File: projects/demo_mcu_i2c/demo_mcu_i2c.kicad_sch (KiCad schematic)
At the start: 9 parts, among them Y1 16MHz

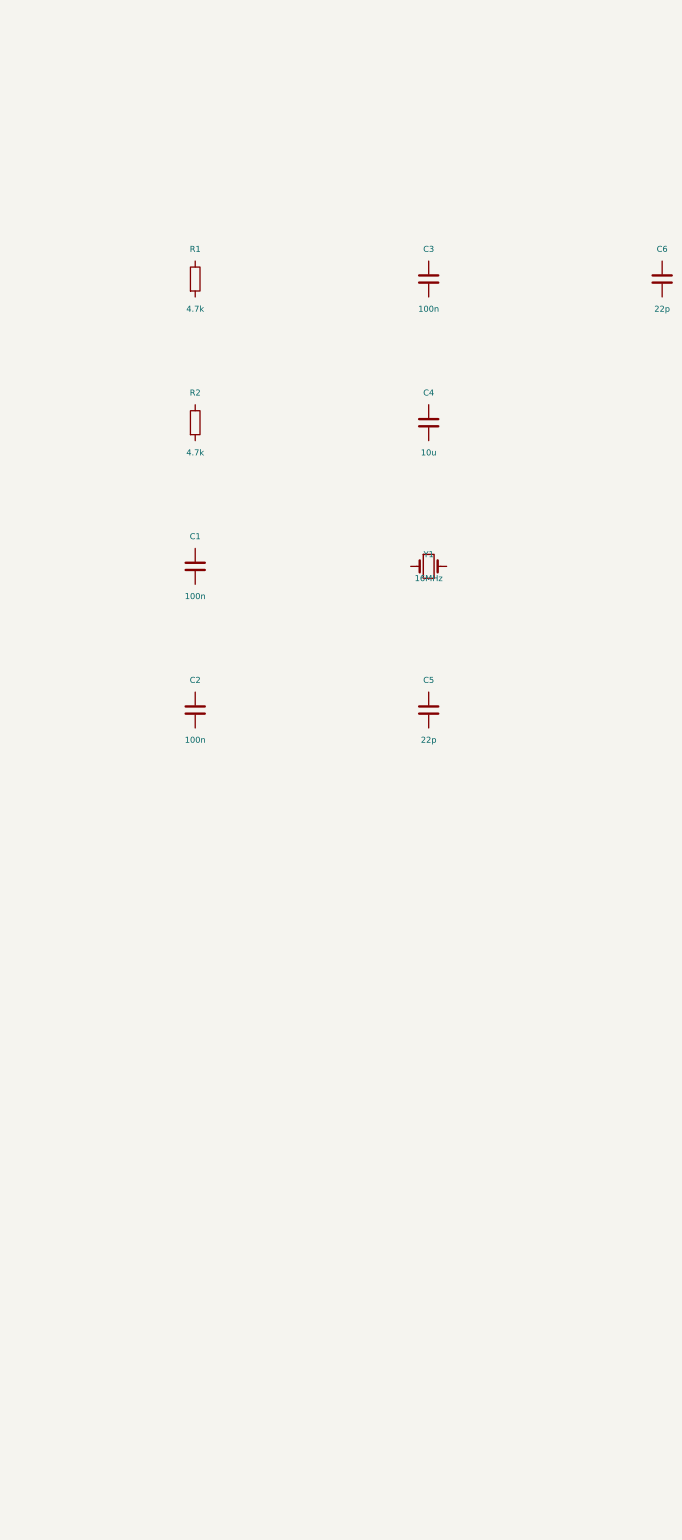
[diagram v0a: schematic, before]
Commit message: Phase 0: KiCad 10 migration + fix blind ERC parsing
- kicad-cli writes JSON reports only to -o file, never stdout; runner
  now uses a temp report file and real JSON decoding
- DetectKicadCLI exported and reused by render_sch and export_test
- KiCad 10 symbol renames (ATmega328-AU -> ATmega328-A) and pin
  numbers fixed in demos

Co-Authored-By: Claude Fable 5 <noreply@anthropic.com>
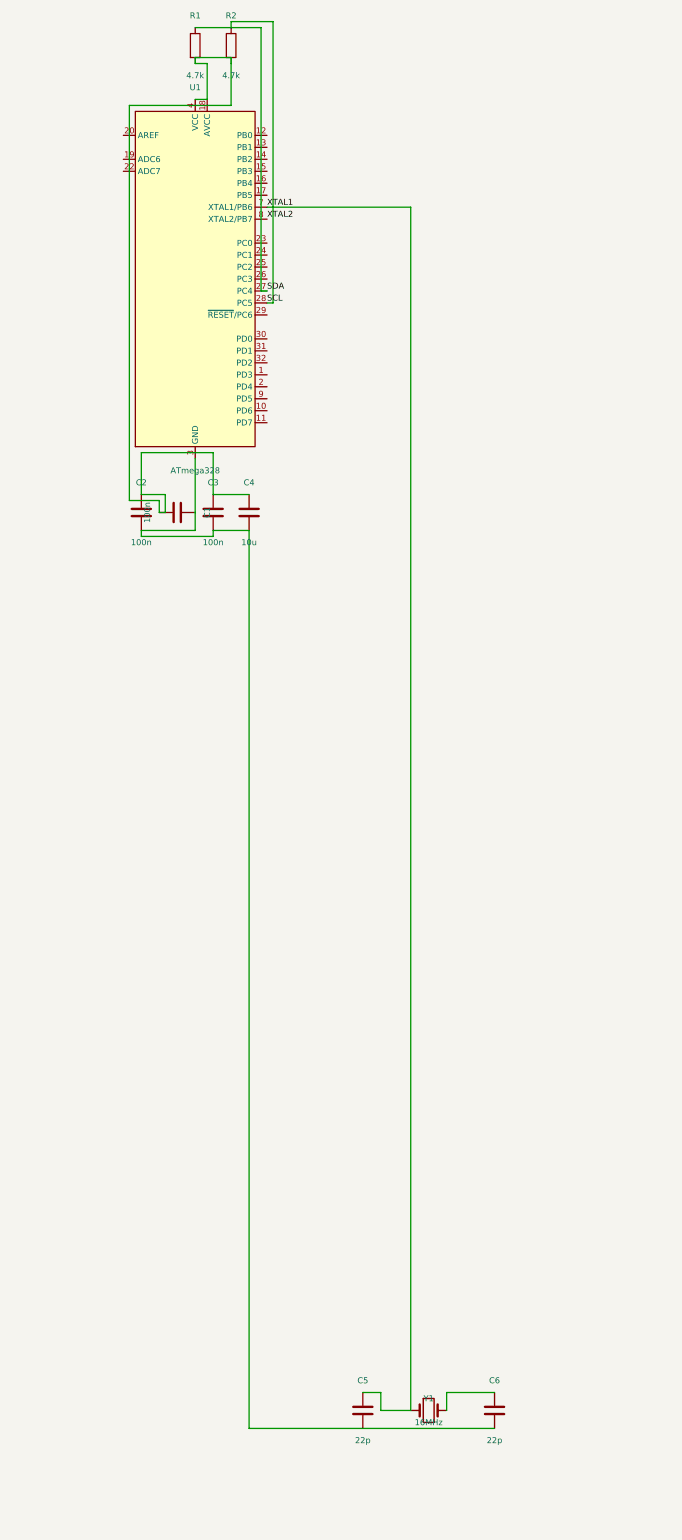
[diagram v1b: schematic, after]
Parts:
- added U1: ATmega328, symbol MCU_Microchip_ATmega:ATmega328-A
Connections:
- net at C6.1: now also Y1.2
- net at C6.2: now also C1.2, C2.2, C3.2, C4.2, C5.2, U1.21 (GND), U1.3 (GND), U1.5 (GND)
- net SDA: now reaches R1.1
- net SDA: now also U1.27 (PC4)
- net at R1.2: now also C1.1, C2.1, C3.1, C4.1, R2.2, U1.18 (AVCC), U1.4 (VCC), U1.6 (VCC)
- net XTAL1: now reaches C5.1
- net XTAL1: now also Y1.1, U1.7 (XTAL1/PB6)
- net SCL: now reaches R2.1
- net SCL: now also U1.28 (PC5)
- new net XTAL2: U1.8 (XTAL2/PB7)

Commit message: Phase 1: geometric quality gate (internal/place2/gate)
Post-hoc Enforce() guarantees zero cross-net crossings, zero wires
through symbol bodies, zero collinear overlaps: offending nets are
demoted to net labels (no geometry, identical connectivity). Wired
into connect_netlist and relayout. Same-net duplicate segments are
merged by Clean, not demoted.

Co-Authored-By: Claude Fable 5 <noreply@anthropic.com>
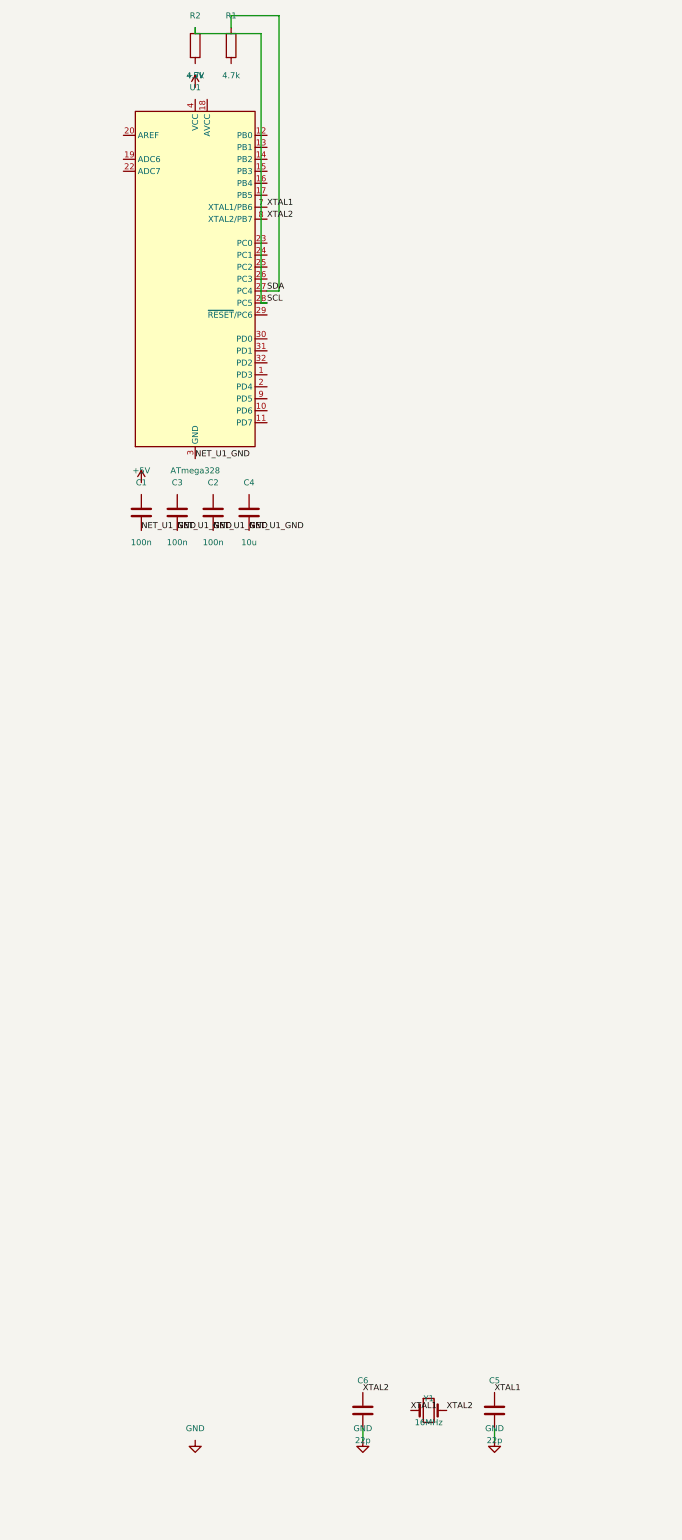
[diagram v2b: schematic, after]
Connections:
- net XTAL2: now also C6.1, Y1.2
- net NET_U1_GND: now reaches C1.2, C2.2, C3.2, C4.2, U1.21 (GND), U1.3 (GND), U1.5 (GND)
- net NET_U1_GND: no longer C5.2, C6.2
- new net: U1.4 (VCC), U1.6 (VCC)
- new net GND: C5.2, C6.2
- now unconnected: C1.1, C2.1, C3.1, C4.1, R1.2, R2.2, U1.18 (AVCC)

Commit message: Phase 3: parametric cluster wiring generators (internal/place2/wiregen)
Closed-form wiring (straight or single-L with clear-corridor
preconditions) for decoupling, 2-pin satellites, dividers and crystal
load caps; generators apply or decline, never search. Integrated as a
pre-pass in connect_netlist with component-aware MST; discovery-label
fallback now also fires for nets fully consumed by wiregen (fixes
dropped-net regression, covered by two regression tests).

Co-Authored-By: Claude Fable 5 <noreply@anthropic.com>
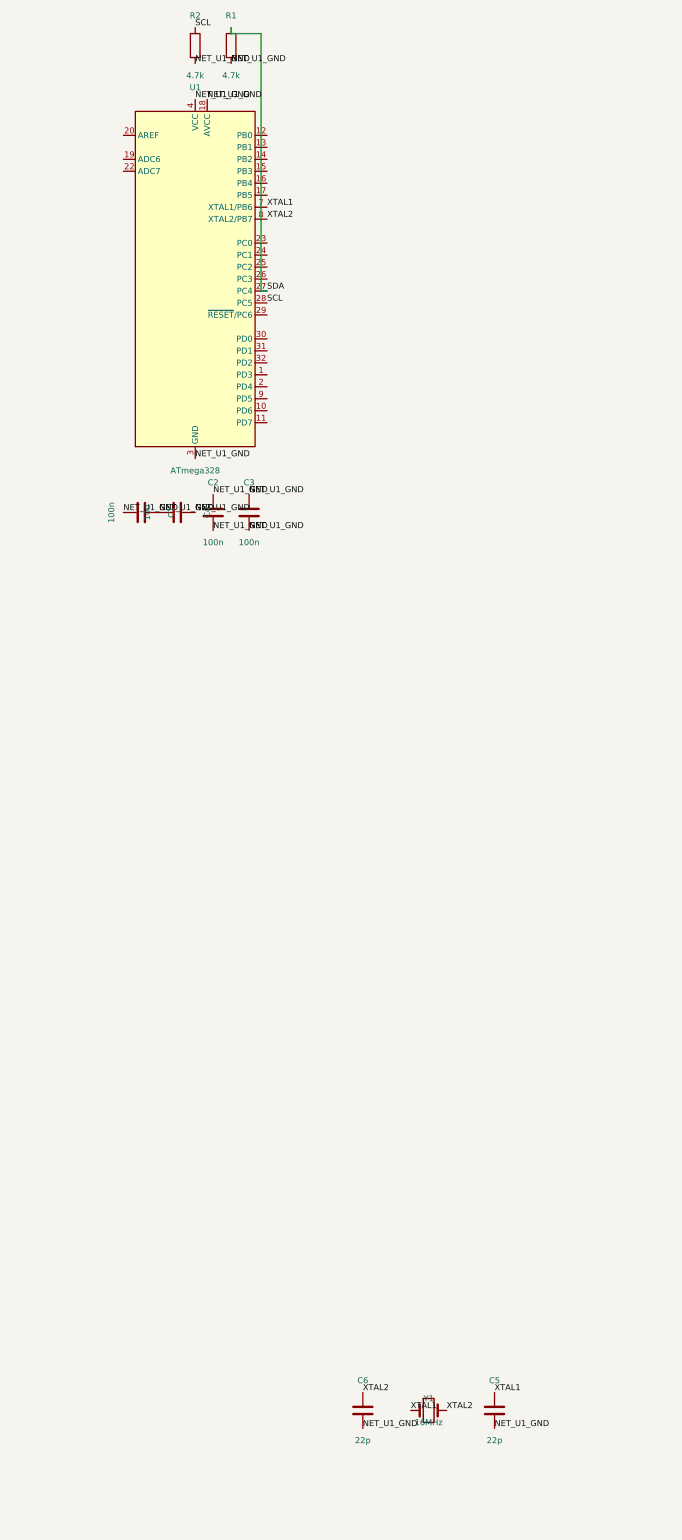
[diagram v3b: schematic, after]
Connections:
- net GND is gone; now on net NET_U1_GND: C5.2, C6.2
- net NET_U1_GND: now also C1.1, C2.1, C3.1, C4.1, R1.2, R2.2, U1.18 (AVCC), U1.4 (VCC), U1.6 (VCC)

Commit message: Phase 4: per-pin power rail policy + full pipeline determinism
Power nets are never routed: every pin on a rail gets its own power
symbol (GND down, VCC up) with a 2.54mm stub; PWR_FLAG emitted after
the gate for undriven power_in nets. Determinism: cluster detection
and TraceNets no longer depend on Go map iteration order (refOrder
slices, sorted canonical net naming). 6/6 identical runs on vreg and
mcu demos; vreg ERC now has zero errors.

Co-Authored-By: Claude Fable 5 <noreply@anthropic.com>
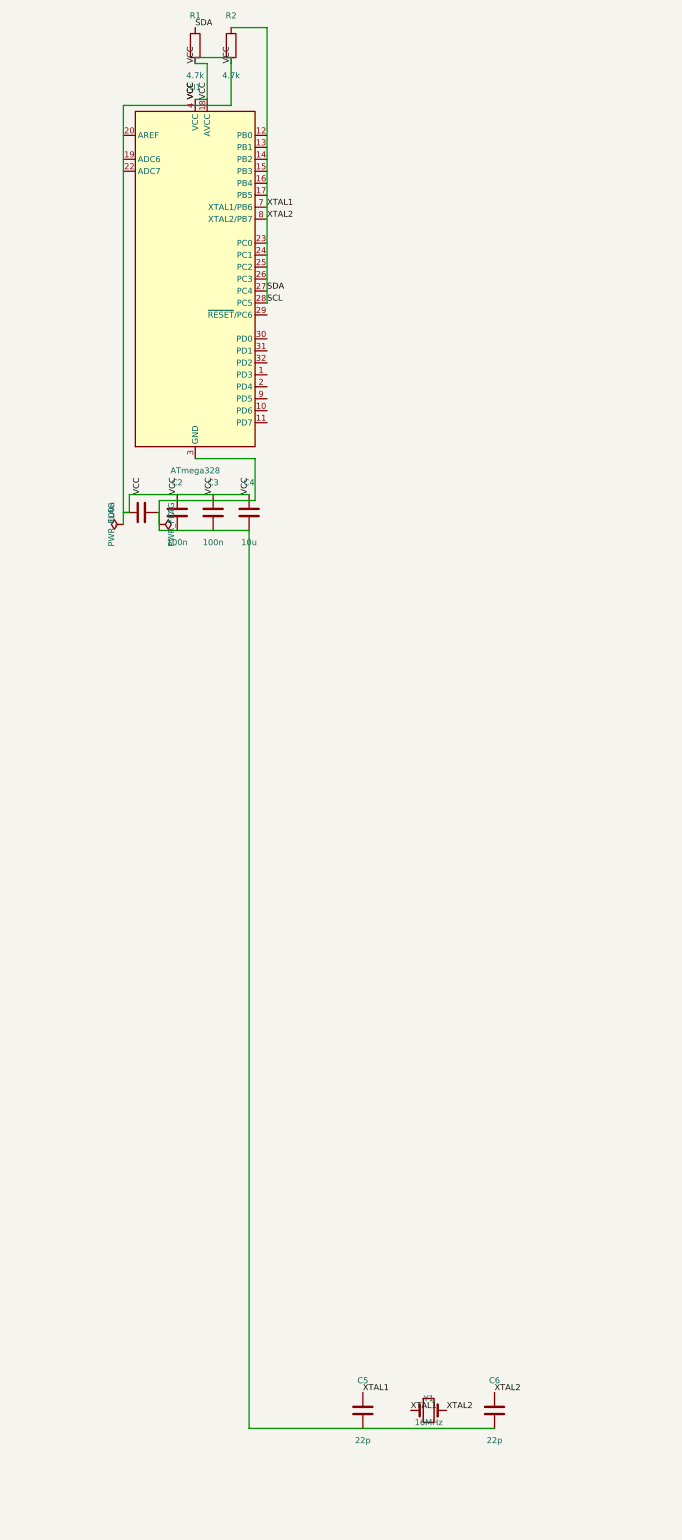
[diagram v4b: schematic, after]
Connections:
- net SDA is gone; now on net SCL: R1.1, U1.27 (PC4)
- net XTAL1 is gone; now on net SCL: C5.1, U1.7 (XTAL1/PB6), Y1.1
- net XTAL2 is gone; now on net SCL: C6.1, U1.8 (XTAL2/PB7), Y1.2
- net NET_U1_GND: no longer names the net of C1.2, C2.2, C3.2, C4.2, C5.2, C6.2, U1.21 (GND), U1.3 (GND), U1.5 (GND)
- net NET_U1_GND: no longer C1.1, C2.1, C3.1, C4.1, R1.2, R2.2, U1.18 (AVCC), U1.4 (VCC), U1.6 (VCC)
- new net VCC: C1.1, C2.1, C3.1, C4.1, R1.2, R2.2, U1.18 (AVCC), U1.4 (VCC), U1.6 (VCC)

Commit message: Phase 4b: fit schematic content to sheet after relayout
Rigid grid-aligned translation of all content into the usable page
area (>=12.7mm margins), avoiding the title block; auto-upgrades
paper A4->A3 when content cannot fit. Known limit: mcu_i2c PlaceFlow
column sprawl (302mm) exceeds A3; placement compaction pending.

Co-Authored-By: Claude Fable 5 <noreply@anthropic.com>
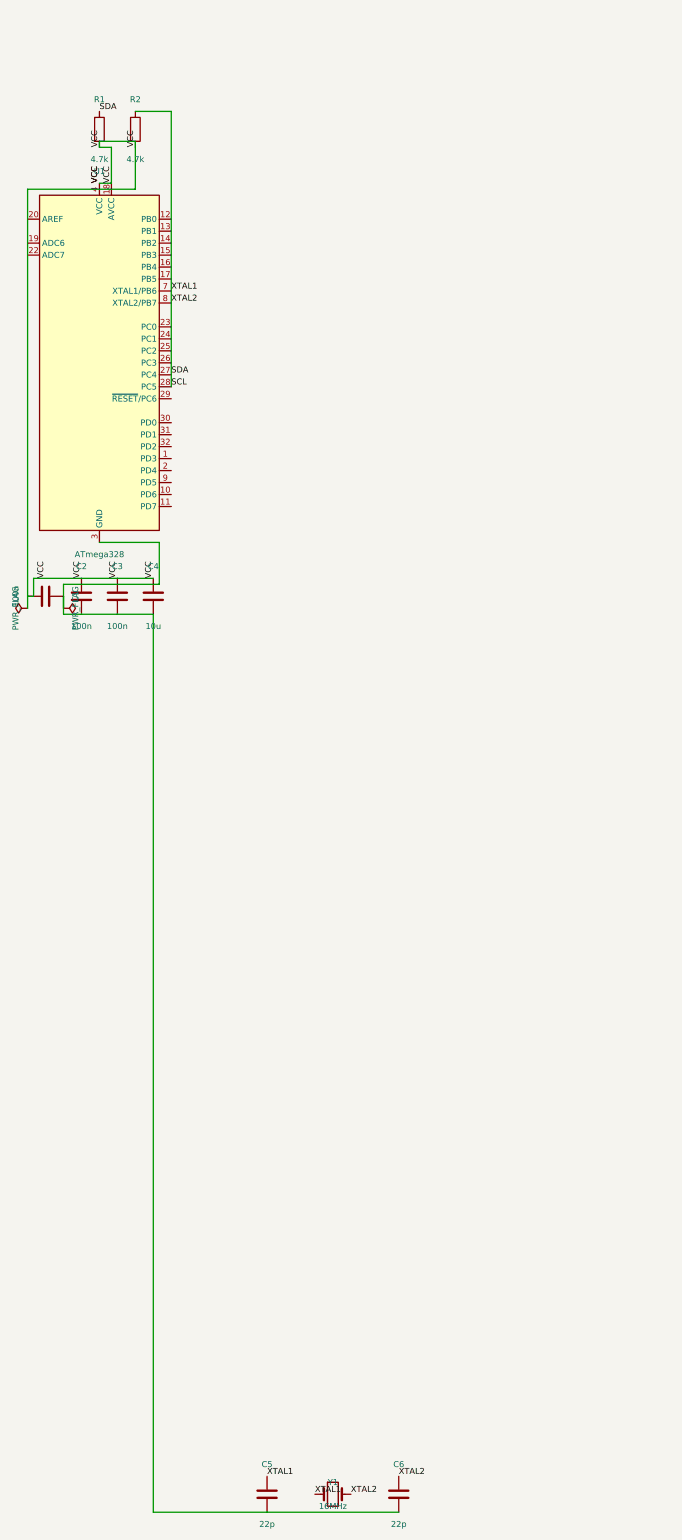
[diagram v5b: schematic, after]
